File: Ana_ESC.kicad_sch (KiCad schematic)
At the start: 0 parts

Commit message: mosfet v2
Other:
- added sheet Mosfetv2 (mosfetv2.kicad_sch)
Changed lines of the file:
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@@
-			)
-		)
-		(pin "Vdrain" input
-			(at 190.5 48.26 180)
-			(effects
-				(font
-					(size 1.27 1.27)
-				)
-				(justify left)
 			)
 		)
@@
 		(pin "SPC" output
 			(at 190.5 106.68 180)
+			(effects
+				(font
+					(size 1.27 1.27)
+				)
+				(justify left)
+			)
+		)
+		(pin "Vdrain" output
+			(at 190.5 48.26 180)
 			(effects
 				(font
@@
 				)
 			)
+		)
+	)
+	(sheet
+		(at 137.16 128.27)
+		(size 31.75 49.53)
+		(exclude_from_sim no)
+		(in_bom yes)
+		(on_board yes)
+		(dnp no)
+		(fields_autoplaced yes)
+		(stroke
+			(width 0.1524)
+			(type solid)
+		)
+		(fill
+			(color 0 0 0 0.0000)
+		)
+		(property "Sheetname" "Mosfetv2"
+			(at 137.16 127.5584 0)
+			(effects
+				(font
+					(size 1.27 1.27)
+				)
+				(justify left bottom)
+			)
+		)
+		(property "Sheetfile" "mosfetv2.kicad_sch"
+			(at 137.16 178.3846 0)
+			(effects
+				(font
+					(size 1.27 1.27)
+				)
+				(justify left top)
+			)
+		)
+		(pin "FAZ_A" output
+			(at 137.16 137.16 180)
+			(effects
+				(font
+					(size 1.27 1.27)
+				)
+				(justify left)
+			)
+		)
+		(pin "FAZ_B" output
+			(at 137.16 139.7 180)
+			(effects
+				(font
+					(size 1.27 1.27)
+				)
+				(justify left)
+			)
+		)
+		(pin "FAZ_C" output
+			(at 137.16 143.51 180)
+			(effects
+				(font
+					(size 1.27 1.27)
+				)
+				(justify left)
+			)
+		)
+		(pin "GHA" input
+			(at 137.16 147.32 180)
+			(effects
+				(font
+					(size 1.27 1.27)
+				)
+				(justify left)
+			)
+		)
+		(pin "GHB" input
+			(at 137.16 149.86 180)
+			(effects
+				(font
+					(size 1.27 1.27)
+				)
+				(justify left)
+			)
+		)
+		(pin "GHC" input
+			(at 137.16 152.4 180)
+			(effects
+				(font
+					(size 1.27 1.27)
+				)
+				(justify left)
+			)
+		)
+		(pin "GLA" input
+			(at 137.16 157.48 180)
+			(effects
+				(font
+					(size 1.27 1.27)
+				)
+				(justify left)
+			)
+		)
+		(pin "GLB" input
+			(at 137.16 160.02 180)
+			(effects
+				(font
+					(size 1.27 1.27)
+				)
+				(justify left)
+			)
+		)
+		(pin "GLC" input
+			(at 137.16 162.56 180)
+			(effects
+				(font
+					(size 1.27 1.27)
+				)
+				(justify left)
+			)
+		)
+		(pin "SHA" output
+			(at 137.16 166.37 180)
+			(effects
+				(font
+					(size 1.27 1.27)
+				)
+				(justify left)
+			)
+		)
+		(pin "SHB" output
+			(at 137.16 168.91 180)
+			(effects
+				(font
+					(size 1.27 1.27)
+				)
+				(justify left)
+			)
+		)
+		(pin "SHC" output
+			(at 137.16 171.45 180)
+			(effects
+				(font
+					(size 1.27 1.27)
+				)
+				(justify left)
+			)
+		)
+		(pin "SNA" output
+			(at 168.91 170.18 0)
+			(effects
+				(font
+					(size 1.27 1.27)
+				)
+				(justify right)
+			)
+		)
+		(pin "SNB" output
+			(at 168.91 168.91 0)
+			(effects
+				(font
+					(size 1.27 1.27)
+				)
+				(justify right)
+			)
+		)
+		(pin "SNC" output
+			(at 168.91 166.37 0)
+			(effects
+				(font
+					(size 1.27 1.27)
+				)
+				(justify right)
+			)
+		)
+		(pin "SPA" output
+			(at 168.91 156.21 0)
+			(effects
+				(font
+					(size 1.27 1.27)
+				)
+				(justify right)
+			)
+		)
+		(pin "SPB" output
+			(at 168.91 153.67 0)
+			(effects
+				(font
+					(size 1.27 1.27)
+				)
+				(justify right)
+			)
+		)
+		(pin "SPC" output
+			(at 168.91 151.13 0)
+			(effects
+				(font
+					(size 1.27 1.27)
+				)
+				(justify right)
+			)
+		)
+		(pin "Vdrain" output
+			(at 168.91 147.32 0)
+			(effects
+				(font
+					(size 1.27 1.27)
+				)
+				(justify right)
+			)
+		)
+		(instances
+			(project "Ana_ESC"
+				(path "/57129761-6d47-486c-bd7a-90dbb6f75754"
+					(page "5")
+				)
+			)

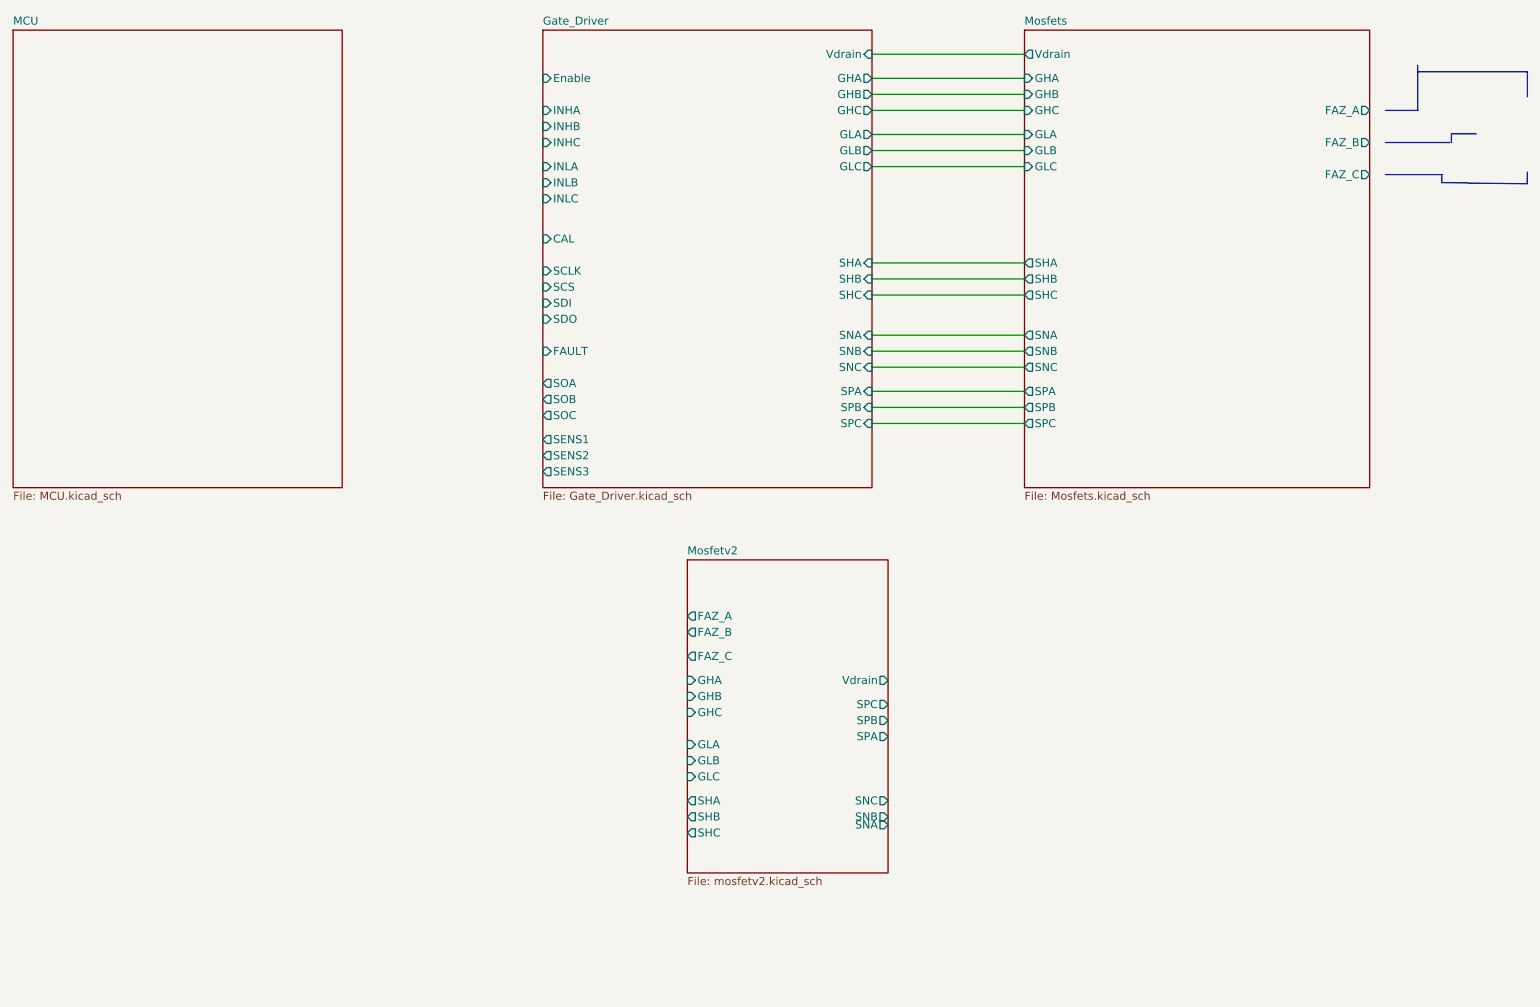
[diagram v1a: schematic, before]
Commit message: MCU schematics update
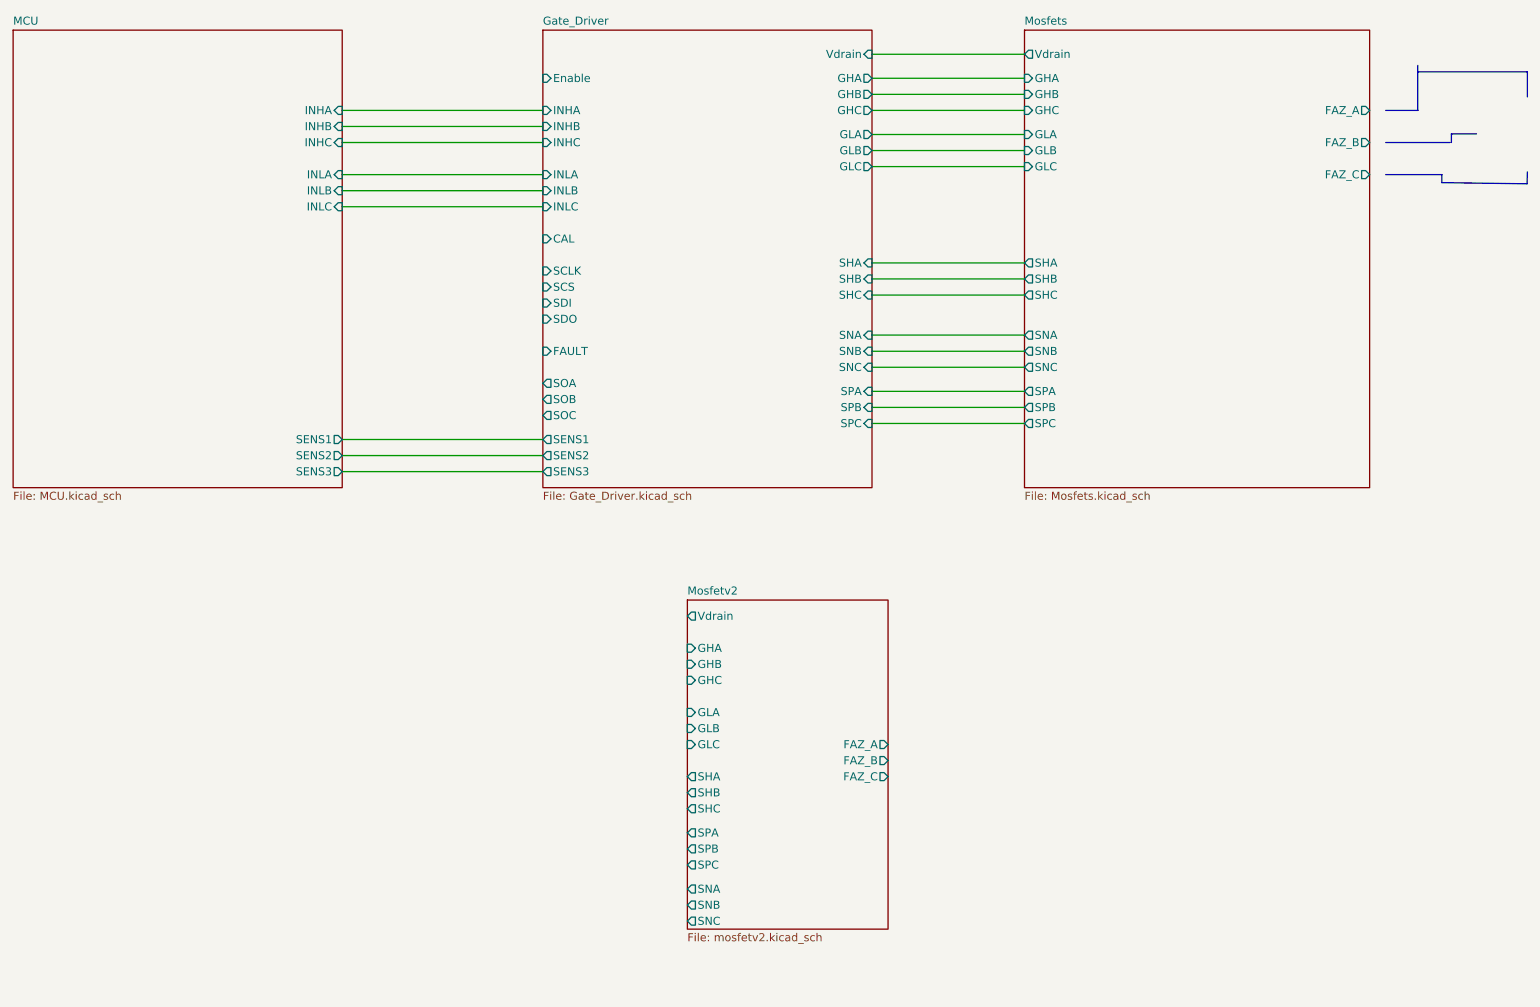
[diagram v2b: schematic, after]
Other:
- sheet MCU ports: added INHA, INHB, INHC, INLA, INLB, INLC, SENS1, SENS2, SENS3; removed none

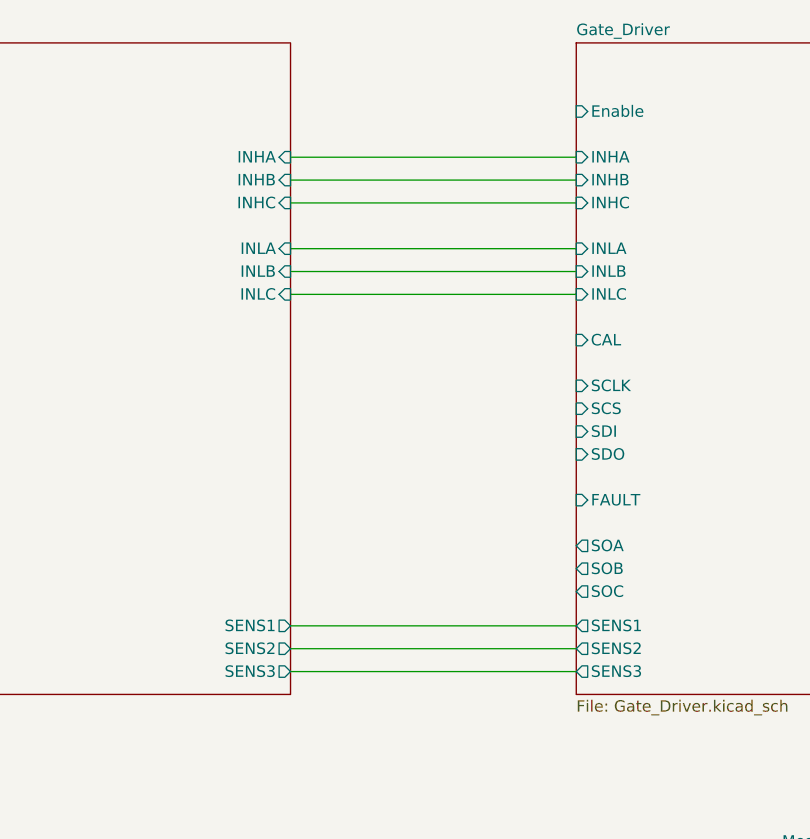
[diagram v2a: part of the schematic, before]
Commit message: some pins changes"
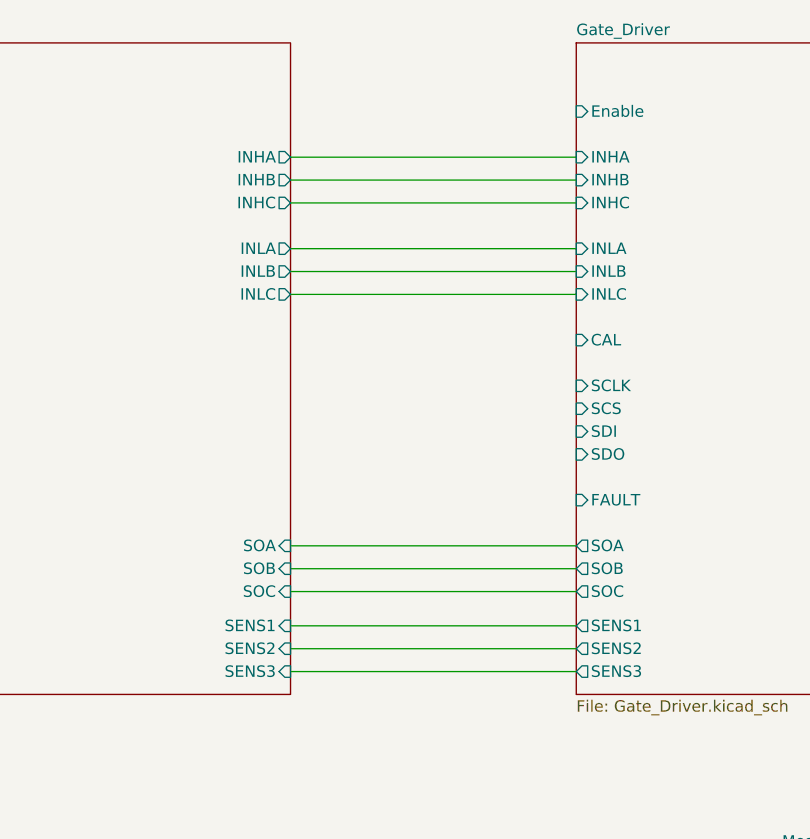
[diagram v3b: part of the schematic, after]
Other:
- sheet MCU ports: added SOA, SOB, SOC; removed none
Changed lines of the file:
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@@
+	(wire
+		(pts
+			(xy 82.55 100.33) (xy 114.3 100.33)
+		)
+		(stroke
+			(width 0)
+			(type default)
+		)
+	)
 	(wire
 		(pts
@@
 	(wire
 		(pts
+			(xy 82.55 102.87) (xy 114.3 102.87)
+		)
+		(stroke
+			(width 0)
+			(type default)
+		)
+	)
+	(wire
+		(pts
 			(xy 166.37 57.15) (xy 190.5 57.15)
 		)
@@
 		(pts
 			(xy 166.37 66.04) (xy 190.5 66.04)
+		)
+		(stroke
+			(width 0)
+			(type default)
+		)
+	)
+	(wire
+		(pts
+			(xy 82.55 105.41) (xy 114.3 105.41)
 		)
 		(stroke
@@
 			)
 		)
-		(pin "INHA" input
+		(pin "INHA" output
 			(at 82.55 57.15 0)
 			(effects
@@
 			)
 		)
-		(pin "INHB" input
+		(pin "INHB" output
 			(at 82.55 59.69 0)
 			(effects
@@
 			)
 		)
-		(pin "INHC" input
+		(pin "INHC" output
 			(at 82.55 62.23 0)
 			(effects
@@
 			)
 		)
-		(pin "INLA" input
+		(pin "INLA" output
 			(at 82.55 67.31 0)
 			(effects
@@
 			)
 		)
-		(pin "INLB" input
+		(pin "INLB" output
 			(at 82.55 69.85 0)
 			(effects
@@
 			)
 		)
-		(pin "INLC" input
+		(pin "INLC" output
 			(at 82.55 72.39 0)
 			(effects
@@
 			)
 		)
-		(pin "SENS1" output
+		(pin "SENS1" input
 			(at 82.55 109.22 0)
 			(effects
@@
 			)
 		)
-		(pin "SENS2" output
+		(pin "SENS2" input
 			(at 82.55 111.76 0)
 			(effects
@@
 			)
 		)
-		(pin "SENS3" output
+		(pin "SENS3" input
 			(at 82.55 114.3 0)
 			(effects
 				(font
+					(size 1.27 1.27)
+				)
+				(justify right)
+			)
+		)
+		(pin "SOA" input
+			(at 82.55 100.33 0)
+			(effects
+				(font
+					(size 1.27 1.27)
+				)
+				(justify right)
+			)
+		)
+		(pin "SOB" input
+			(at 82.55 102.87 0)
+			(effects
+				(font
+					(size 1.27 1.27)
+				)
+				(justify right)
+			)
+		)
+		(pin "SOC" input
+			(at 82.55 105.41 0)
+			(effects
+				(font

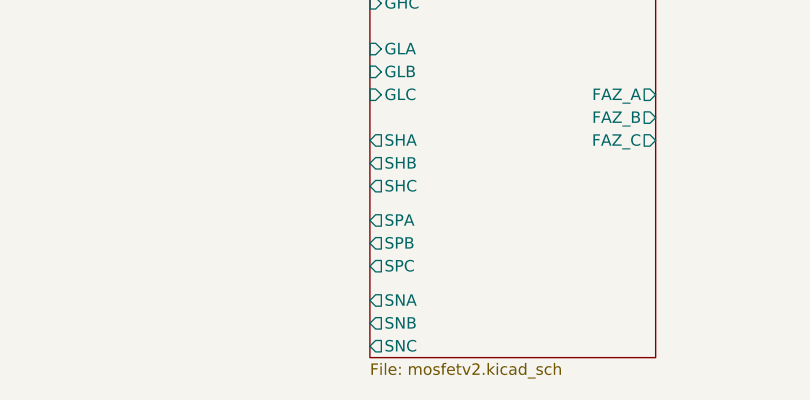
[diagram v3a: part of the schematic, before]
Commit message: thermal calculations done and Shunt Resistors changed. Not 3, just 2 resistors can dissipate the power.
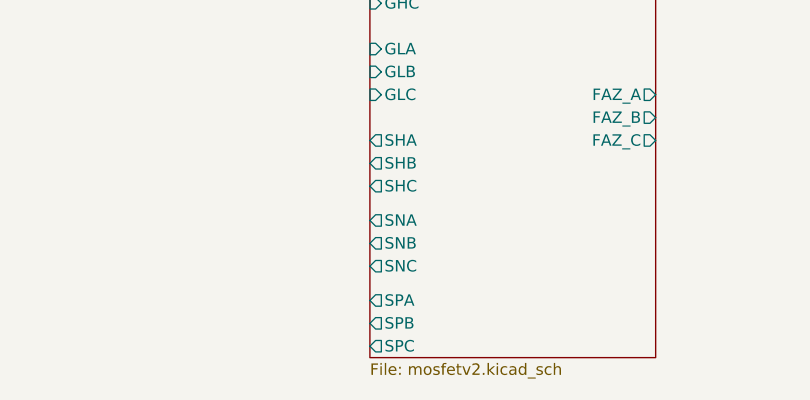
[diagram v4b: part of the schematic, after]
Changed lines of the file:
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@@
 		)
 		(pin "SNA" output
+			(at 137.16 171.45 180)
+			(effects
+				(font
+					(size 1.27 1.27)
+				)
+				(justify left)
+			)
+		)
+		(pin "SNB" output
+			(at 137.16 173.99 180)
+			(effects
+				(font
+					(size 1.27 1.27)
+				)
+				(justify left)
+			)
+		)
+		(pin "SNC" output
+			(at 137.16 176.53 180)
+			(effects
+				(font
+					(size 1.27 1.27)
+				)
+				(justify left)
+			)
+		)
+		(pin "SPA" output
 			(at 137.16 180.34 180)
 			(effects
@@
 			)
 		)
-		(pin "SNB" output
+		(pin "SPB" output
 			(at 137.16 182.88 180)
 			(effects
@@
 			)
 		)
-		(pin "SNC" output
+		(pin "SPC" output
 			(at 137.16 185.42 180)
 			(effects
 				(font
-					(size 1.27 1.27)
-				)
-				(justify left)
-			)
-		)
-		(pin "SPA" output
-			(at 137.16 171.45 180)
-			(effects
-				(font
-					(size 1.27 1.27)
-				)
-				(justify left)
-			)
-		)
-		(pin "SPB" output
-			(at 137.16 173.99 180)
-			(effects
-				(font
-					(size 1.27 1.27)
-				)
-				(justify left)
-			)
-		)
-		(pin "SPC" output
-			(at 137.16 176.53 180)
-			(effects
-				(font
